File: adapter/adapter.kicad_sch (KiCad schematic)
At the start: 50 parts, among them J1 Serial, J10 Ribbon, J11 Ribbon, J12 RGB, J2 Battery charge, J3 Ribbon, J4 Ribbon, J5 RGB, J8 Serial, J9 Battery charge, SW1 SW_SPST, SW2 SW_SPST, SW3 SW_SPDT, SW4 SW_SPDT, U1 Dual MCU: RP2040 + nice!nano, U2 AP1603WG-7, U3 USBLC6-2P6, U4 AP1603WG-7, U5 Dual MCU: RP2040 + nice!nano, U6 USBLC6-2P6

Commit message: sch: use different trrs footprint
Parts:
- J1, J8: footprint library:Jack_3.5mm_PJ320E_Horizontal -> PCM_marbastlib-xp-various:CON_MJ-4PP-9
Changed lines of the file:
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@@
 			)
 		)
-		(property "Footprint" "library:Jack_3.5mm_PJ320E_Horizontal"
+		(property "Footprint" "PCM_marbastlib-xp-various:CON_MJ-4PP-9"
 			(at 137.16 142.24 0)
 			(effects
@@
 			)
 		)
-		(property "Footprint" "library:Jack_3.5mm_PJ320E_Horizontal"
+		(property "Footprint" "PCM_marbastlib-xp-various:CON_MJ-4PP-9"
 			(at 341.63 142.24 0)
 			(effects

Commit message: pcb: use switch
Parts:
- SW3: footprint Button_Switch_SMD:SW_SPDT_PCM12 -> library:200AWMSP2T2A1M6RE
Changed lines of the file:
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@@
 			)
 		)
-		(property "Footprint" "Button_Switch_SMD:SW_SPDT_PCM12"
+		(property "Footprint" "library:200AWMSP2T2A1M6RE"
 			(at 152.4 55.88 0)
 			(effects

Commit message: pcb: use trrs with no bottom hole
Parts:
- J1, J8: footprint PCM_marbastlib-xp-various:CON_MJ-4PP-9 -> library:CON_MJ-4PP-9-no-bottom-hole
- SW4: footprint Button_Switch_SMD:SW_SPDT_PCM12 -> library:200AWMSP2T2A1M6RE
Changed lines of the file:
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@@
 			)
 		)
-		(property "Footprint" "Button_Switch_SMD:SW_SPDT_PCM12"
+		(property "Footprint" "library:200AWMSP2T2A1M6RE"
 			(at 356.87 55.88 0)
 			(effects
@@
 			)
 		)
-		(property "Footprint" "PCM_marbastlib-xp-various:CON_MJ-4PP-9"
+		(property "Footprint" "library:CON_MJ-4PP-9-no-bottom-hole"
 			(at 137.16 142.24 0)
 			(effects
@@
 			)
 		)
-		(property "Footprint" "PCM_marbastlib-xp-various:CON_MJ-4PP-9"
+		(property "Footprint" "library:CON_MJ-4PP-9-no-bottom-hole"
 			(at 341.63 142.24 0)
 			(effects

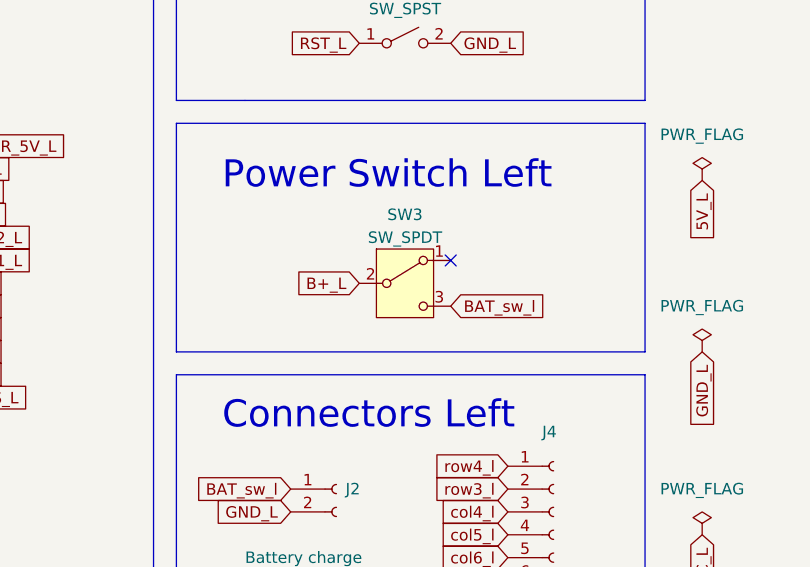
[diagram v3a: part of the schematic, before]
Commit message: pcb: use vertical switch
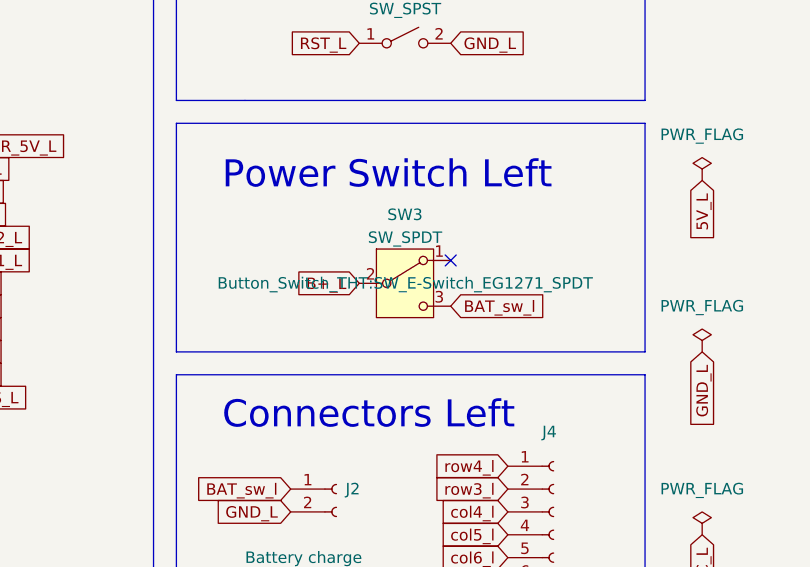
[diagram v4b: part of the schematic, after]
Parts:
- SW3, SW4: footprint library:200AWMSP2T2A1M6RE -> Button_Switch_THT:SW_E-Switch_EG1271_SPDT
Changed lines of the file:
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@@
 			)
 		)
-		(property "Footprint" "library:200AWMSP2T2A1M6RE"
+		(property "Footprint" "Button_Switch_THT:SW_E-Switch_EG1271_SPDT"
 			(at 356.87 55.88 0)
 			(effects
@@
 			)
 		)
-		(property "Footprint" "library:200AWMSP2T2A1M6RE"
+		(property "Footprint" "Button_Switch_THT:SW_E-Switch_EG1271_SPDT"
 			(at 152.4 55.88 0)
 			(effects
@@
 					(size 1.27 1.27)
 				)
-				(hide yes)
-			)
-		)
+			)
+		)

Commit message: pcb: update the trrs footprint
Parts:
- J1, J8: footprint library:CON_MJ-4PP-9-no-bottom-hole -> PCM_marbastlib-xp-various:CON_MJ-4PP-9
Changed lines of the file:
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@@
 			)
 		)
-		(property "Footprint" "library:CON_MJ-4PP-9-no-bottom-hole"
+		(property "Footprint" "PCM_marbastlib-xp-various:CON_MJ-4PP-9"
 			(at 137.16 142.24 0)
 			(effects
@@
 			)
 		)
-		(property "Footprint" "library:CON_MJ-4PP-9-no-bottom-hole"
+		(property "Footprint" "PCM_marbastlib-xp-various:CON_MJ-4PP-9"
 			(at 341.63 142.24 0)
 			(effects

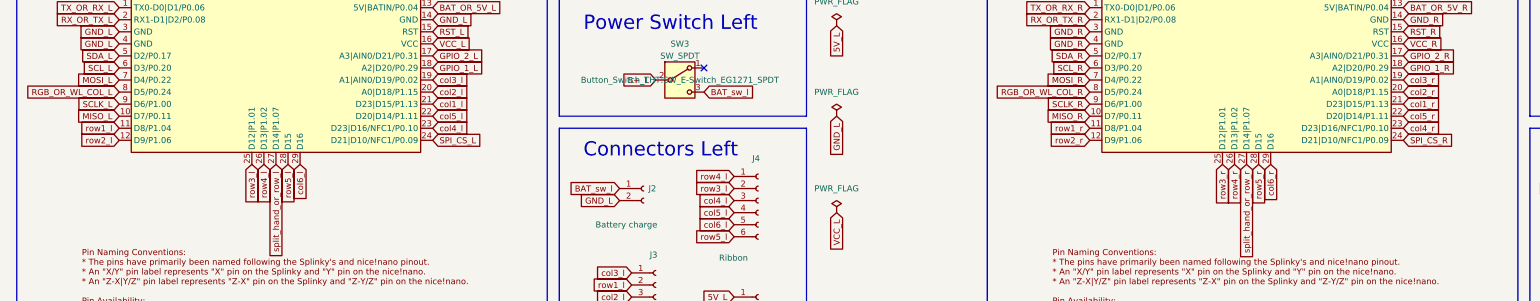
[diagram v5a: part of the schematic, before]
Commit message: sch: replace rows and cols for convenient routing
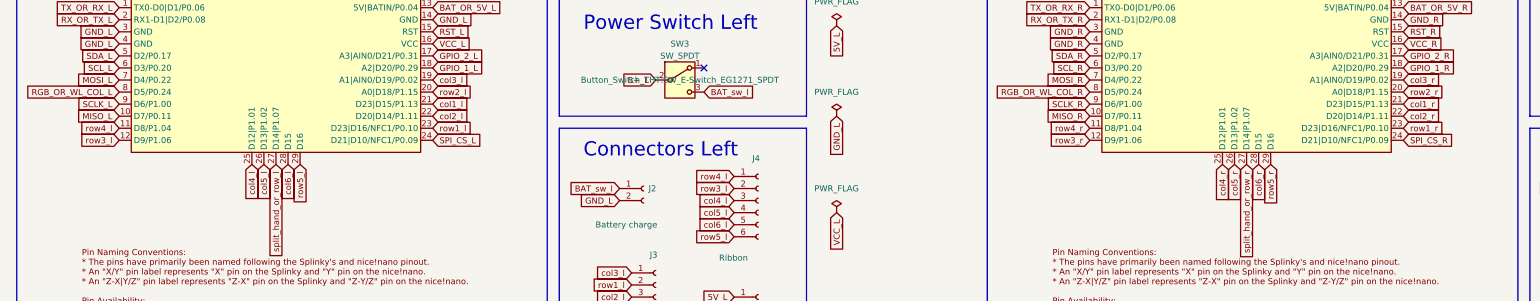
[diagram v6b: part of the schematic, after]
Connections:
- net col2_l: now also U1.22 (D20|D14/P1.11); no longer U1.20 (A0|D18/P1.15)
- net col2_r: now also U5.22 (D20|D14/P1.11); no longer U5.20 (A0|D18/P1.15)
- net col4_l: now also U1.25 (D12|P1.01); no longer U1.23 (D23|D16/NFC1/P0.10)
- net col4_r: now also U5.25 (D12|P1.01); no longer U5.23 (D23|D16/NFC1/P0.10)
- net col5_l: now also U1.26 (D13|P1.02); no longer U1.22 (D20|D14/P1.11)
- net col5_r: now also U5.26 (D13|P1.02); no longer U5.22 (D20|D14/P1.11)
- net col6_l: now also U1.28 (D15); no longer U1.29 (D16)
- net col6_r: now also U5.28 (D15); no longer U5.29 (D16)
- net row1_l: now also U1.23 (D23|D16/NFC1/P0.10); no longer U1.11 (D8/P1.04)
- net row1_r: now also U5.23 (D23|D16/NFC1/P0.10); no longer U5.11 (D8/P1.04)
- net row2_l: now also U1.20 (A0|D18/P1.15); no longer U1.12 (D9/P1.06)
- net row2_r: now also U5.20 (A0|D18/P1.15); no longer U5.12 (D9/P1.06)
- net row3_l: now also U1.12 (D9/P1.06); no longer U1.25 (D12|P1.01)
- net row3_r: now also U5.12 (D9/P1.06); no longer U5.25 (D12|P1.01)
- net row4_l: now also U1.11 (D8/P1.04); no longer U1.26 (D13|P1.02)
- net row4_r: now also U5.11 (D8/P1.04); no longer U5.26 (D13|P1.02)
- net row5_l: now also U1.29 (D16); no longer U1.28 (D15)
- net row5_r: now also U5.29 (D16); no longer U5.28 (D15)

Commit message: sch: fix names of boxes
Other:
- note added: "Connectors Right"
- note added: "Jumpers Right"
- note added: "Level Booster Right"
- note added: "Power Switch Right"
- note added: "Reset button Right"
- note added: "TRRS Right"
- note added: "VIK Connector Right"
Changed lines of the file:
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@@
 		)
 	)
-	(text "Jumpers Left"
+	(text "Jumpers Right"
 		(exclude_from_sim no)
 		(at 242.57 187.96 0)
@@
 		)
 	)
-	(text "Connectors Left"
+	(text "Connectors Right"
 		(exclude_from_sim no)
 		(at 336.55 72.39 0)
@@
 		)
 	)
-	(text "Reset button Left"
+	(text "Reset button Right"
 		(exclude_from_sim no)
 		(at 336.55 19.05 0)
@@
 		)
 	)
-	(text "Level Booster Left"
+	(text "Level Booster Right"
 		(exclude_from_sim no)
 		(at 224.79 120.65 0)
@@
 		)
 	)
-	(text "Power Switch Left"
+	(text "Power Switch Right"
 		(exclude_from_sim no)
 		(at 336.55 45.72 0)
@@
 		)
 	)
-	(text "VIK Connector Left"
+	(text "VIK Connector Right"
 		(exclude_from_sim no)
 		(at 312.42 193.04 0)
@@
 		)
 	)
-	(text "TRRS Left"
+	(text "TRRS Right"
 		(exclude_from_sim no)
 		(at 336.55 127 0)

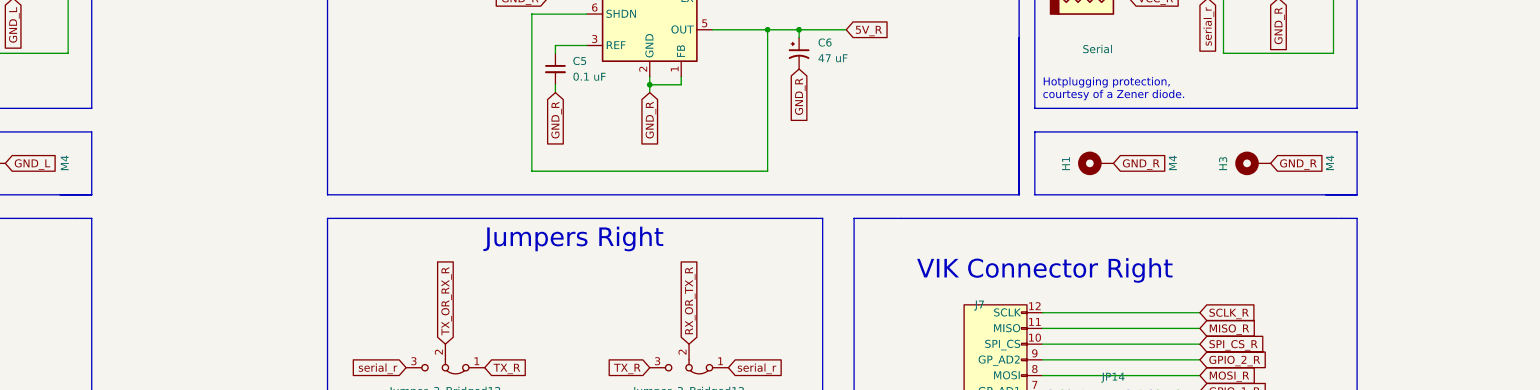
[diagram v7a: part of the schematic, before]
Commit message: pcb: add mousebites
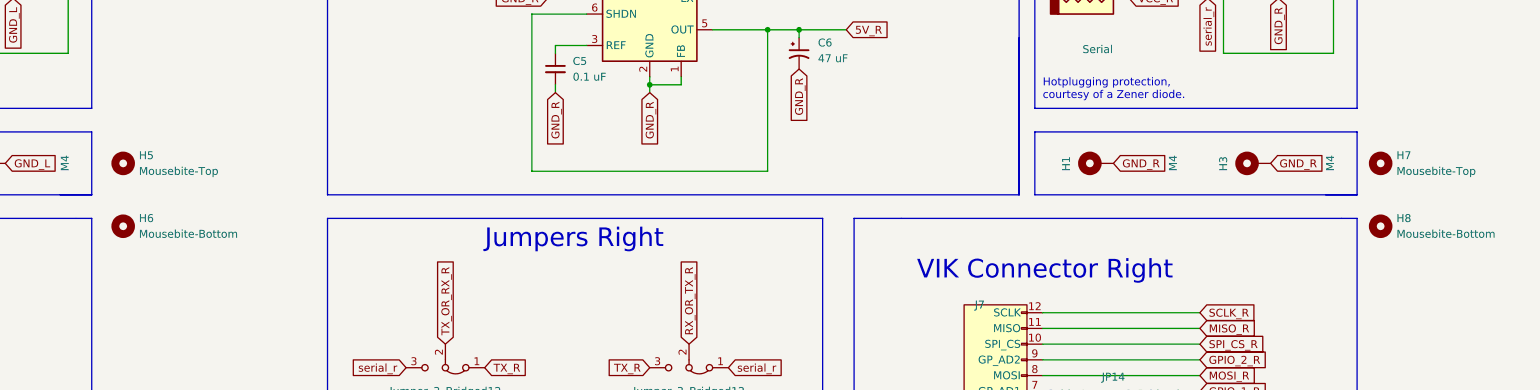
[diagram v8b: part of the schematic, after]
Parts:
- added H5, H7: Mousebite-Top, library:mousebites, symbol Mechanical:MountingHole
- added H6, H8: Mousebite-Bottom, library:mousebites, symbol Mechanical:MountingHole
